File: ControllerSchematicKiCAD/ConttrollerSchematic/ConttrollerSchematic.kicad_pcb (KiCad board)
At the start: 2 copper layers, 174 x 42 mm, 8 parts

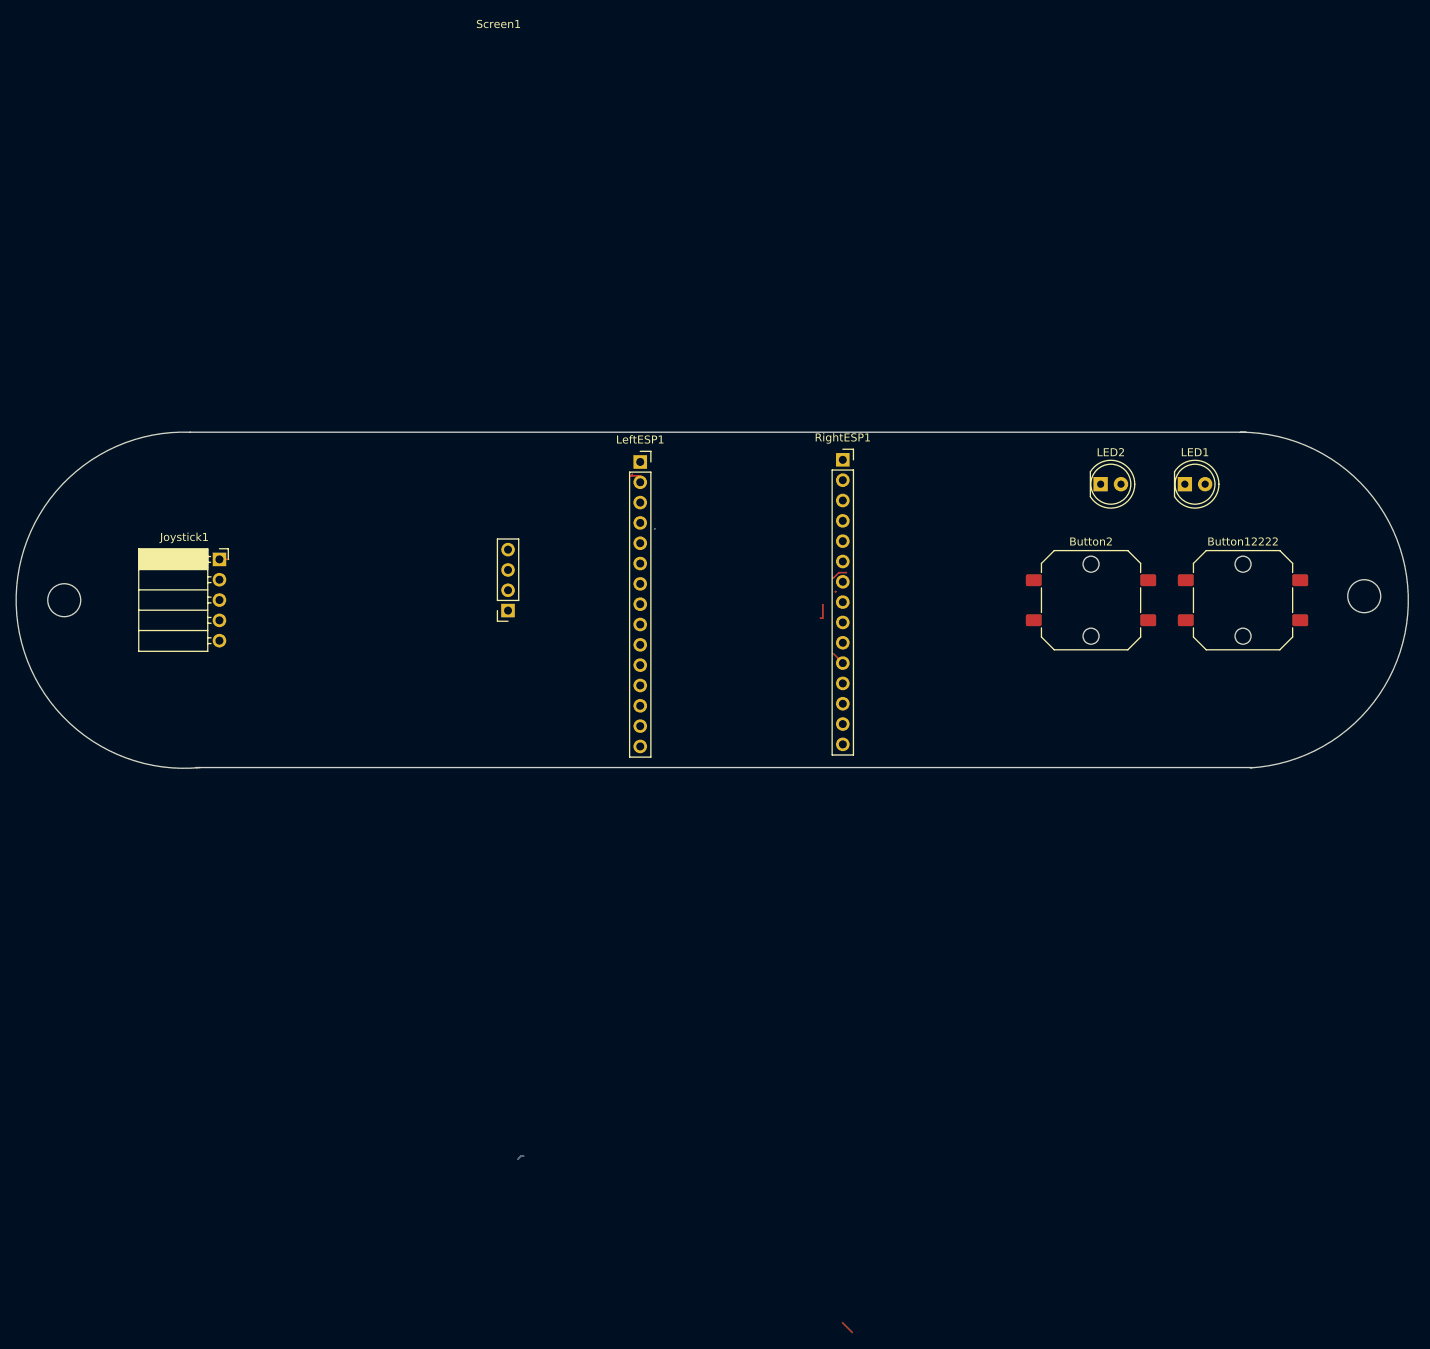
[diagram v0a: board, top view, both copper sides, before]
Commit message: imported from 3d model for exact dimensions
I imported the dxf from the model for the controller and then I made that the edge cuts for the board. I also added some art
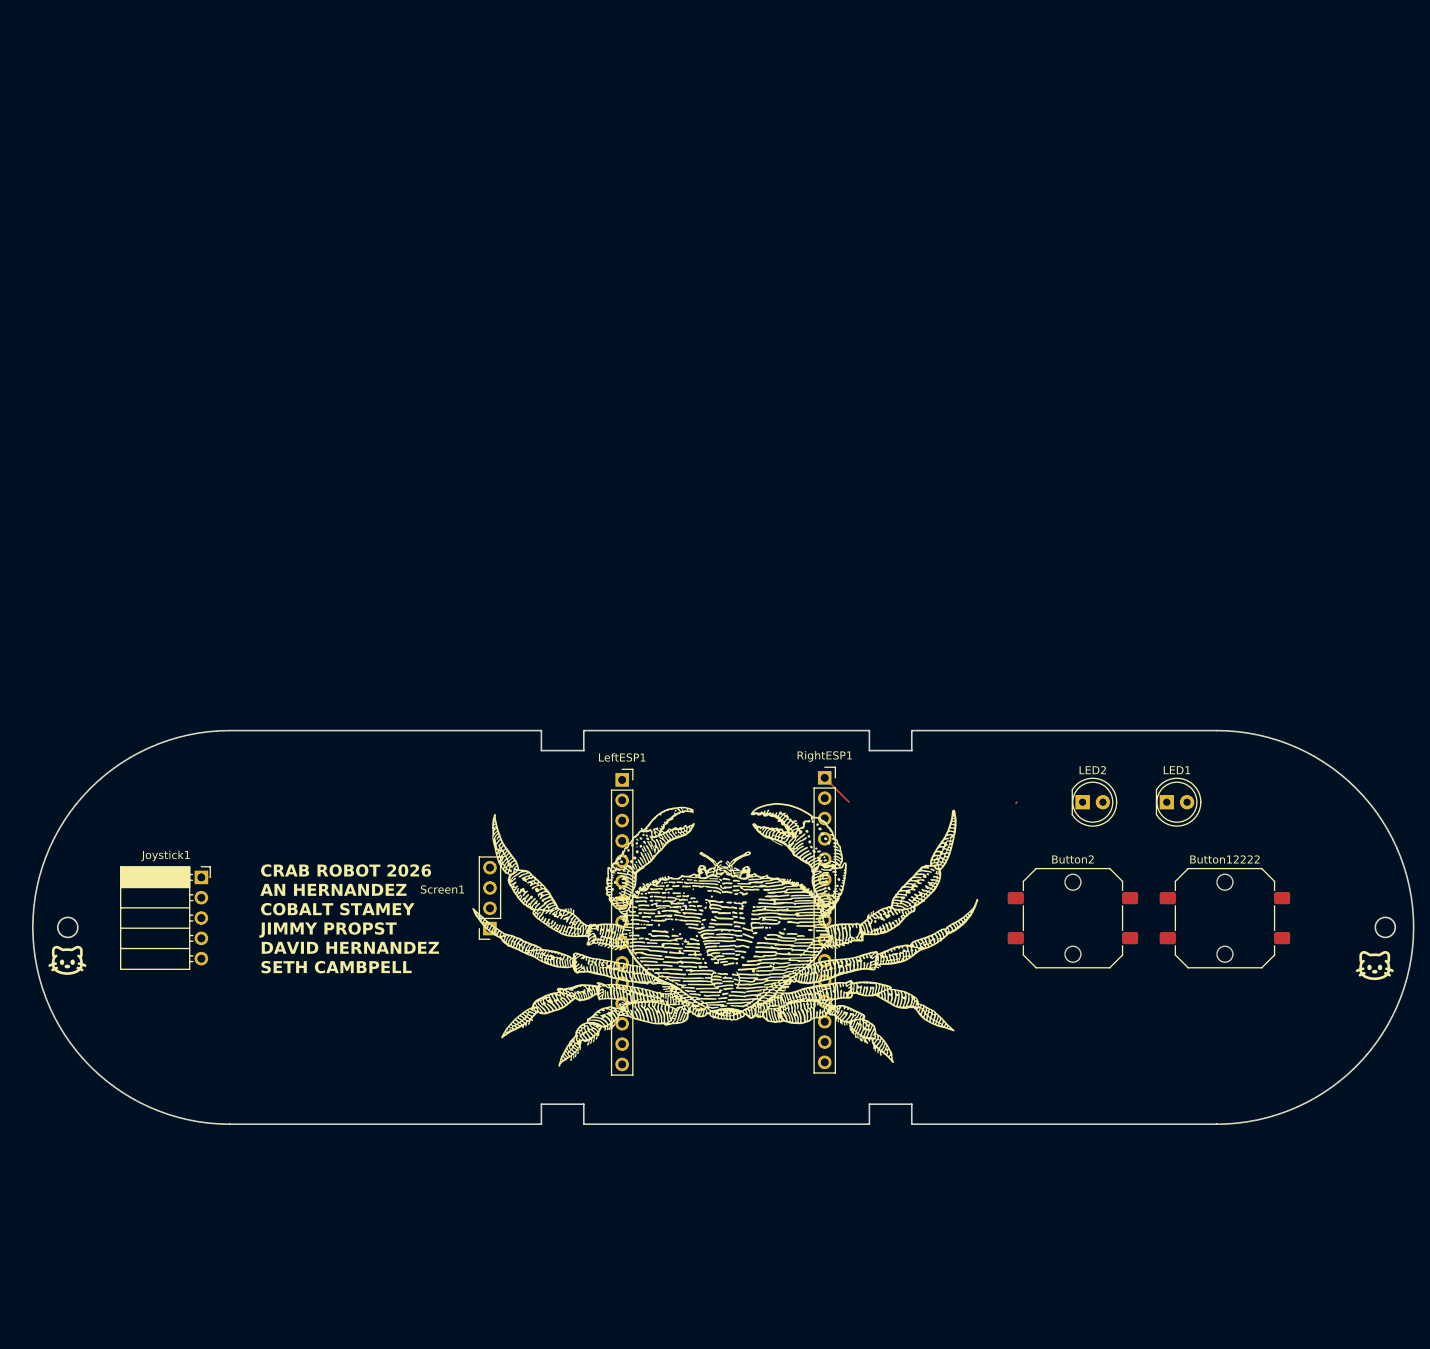
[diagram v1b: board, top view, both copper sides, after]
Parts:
- moved Joystick1 39.8 mm to (86.6, 93.7)
- moved Button12222 39.8 mm to (214.6, 98.8)
- moved Button2 39.8 mm to (195.6, 98.8)
- moved LED1 39.8 mm to (207.3, 84.2)
- moved LED2 39.8 mm to (196.8, 84.2)
- moved LeftESP1 39.8 mm to (139.2, 81.5)
- moved Screen1 39.8 mm to (122.7, 100.0)
- moved RightESP1 39.8 mm to (164.6, 81.2)
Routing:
- net unconnected-(RightESP1-Pin_9-Pad9): track 4.06 -> 0.00 mm
- net GND: track 2.27 -> 4.53 mm
- net /R11: track 1.99 -> 0.27 mm
- net /R14: track 2.52 -> 1.62 mm
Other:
- board size 174 x 42 mm -> 172.6 x 49.2 mm
- board text added: "CRAB ROBOT 2026 AN HERNANDEZ COBALT STAMEY JIMMY PROPST DAVID HERNANDEZ SETH CAMBPELL"
